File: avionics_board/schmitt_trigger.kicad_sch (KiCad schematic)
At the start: 3 parts, among them U55 74LVC2G07

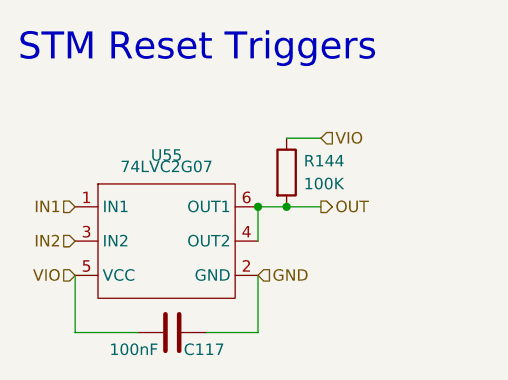
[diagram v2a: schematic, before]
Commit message: cleaning up bom: remove main camera port since it has not pullups and capacitors, correcting some errors in camera switch
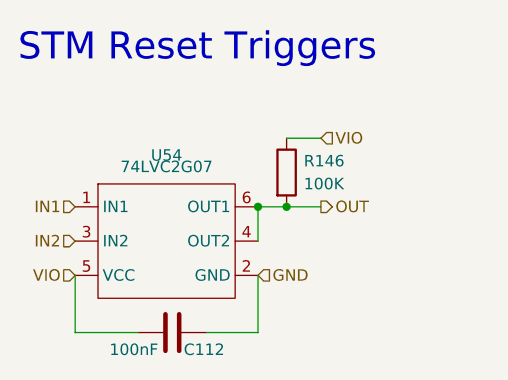
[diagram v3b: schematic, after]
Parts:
- renumbered C117 to C112, R144 to R146, U55 to U54
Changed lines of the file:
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@@
 		(dnp no)
 		(fields_autoplaced yes)
-		(property "Reference" "U55"
+		(property "Reference" "U54"
 			(at 214.63 69.85 0)
 			(effects
@@
 		)
 		(property "Color" ""
+			(at 214.63 79.375 0)
+			(effects
+				(font
+					(size 1.27 1.27)
+				)
+				(hide yes)
+			)
+		)
+		(property "MANUFACTURER" ""
+			(at 214.63 79.375 0)
+			(effects
+				(font
+					(size 1.27 1.27)
+				)
+				(hide yes)
+			)
+		)
+		(property "MAXIMUM_PACKAGE_HEIGHT" ""
+			(at 214.63 79.375 0)
+			(effects
+				(font
+					(size 1.27 1.27)
+				)
+				(hide yes)
+			)
+		)
+		(property "Manufactorer" ""
+			(at 214.63 79.375 0)
+			(effects
+				(font
+					(size 1.27 1.27)
+				)
+				(hide yes)
+			)
+		)
+		(property "PARTREV" ""
+			(at 214.63 79.375 0)
+			(effects
+				(font
+					(size 1.27 1.27)
+				)
+				(hide yes)
+			)
+		)
+		(property "STANDARD" ""
 			(at 214.63 79.375 0)
 			(effects
@@
 			(project "EPS"
 				(path "/05170af6-30ef-4c3a-b972-f098085da1bc/3cb52b52-bdd8-455c-8cb1-f3a303a9432e"
-					(reference "U55")
+					(reference "U54")
 					(unit 1)
 				)
@@
 		(on_board yes)
 		(dnp no)
-		(property "Reference" "C117"
+		(property "Reference" "C112"
 			(at 216.535 91.44 90)
 			(effects
@@
 		)
 		(property "Color" ""
+			(at 215.265 89.535 0)
+			(effects
+				(font
+					(size 1.27 1.27)
+				)
+				(hide yes)
+			)
+		)
+		(property "MANUFACTURER" ""
+			(at 215.265 89.535 0)
+			(effects
+				(font
+					(size 1.27 1.27)
+				)
+				(hide yes)
+			)
+		)
+		(property "MAXIMUM_PACKAGE_HEIGHT" ""
+			(at 215.265 89.535 0)
+			(effects
+				(font
+					(size 1.27 1.27)
+				)
+				(hide yes)
+			)
+		)
+		(property "Manufactorer" ""
+			(at 215.265 89.535 0)
+			(effects
+				(font
+					(size 1.27 1.27)
+				)
+				(hide yes)
+			)
+		)
+		(property "PARTREV" ""
+			(at 215.265 89.535 0)
+			(effects
+				(font
+					(size 1.27 1.27)
+				)
+				(hide yes)
+			)
+		)
+		(property "STANDARD" ""
 			(at 215.265 89.535 0)
 			(effects
@@
 			(project "EPS"
 				(path "/05170af6-30ef-4c3a-b972-f098085da1bc/3cb52b52-bdd8-455c-8cb1-f3a303a9432e"
-					(reference "C117")
+					(reference "C112")
 					(unit 1)
 				)
@@
 		(dnp no)
 		(fields_autoplaced yes)
-		(property "Reference" "R144"
+		(property "Reference" "R146"
 			(at 229.87 70.4849 0)
 			(effects
@@
 		)
 		(property "Color" ""
+			(at 227.965 71.755 0)
+			(effects
+				(font
+					(size 1.27 1.27)
+				)
+				(hide yes)
+			)
+		)
+		(property "MANUFACTURER" ""
+			(at 227.965 71.755 0)
+			(effects
+				(font
+					(size 1.27 1.27)
+				)
+				(hide yes)
+			)
+		)
+		(property "MAXIMUM_PACKAGE_HEIGHT" ""
+			(at 227.965 71.755 0)
+			(effects
+				(font
+					(size 1.27 1.27)
+				)
+				(hide yes)
+			)
+		)
+		(property "Manufactorer" ""
+			(at 227.965 71.755 0)
+			(effects
+				(font
+					(size 1.27 1.27)
+				)
+				(hide yes)
+			)
+		)
+		(property "PARTREV" ""
+			(at 227.965 71.755 0)
+			(effects
+				(font
+					(size 1.27 1.27)
+				)
+				(hide yes)
+			)
+		)
+		(property "STANDARD" ""
 			(at 227.965 71.755 0)
 			(effects
@@
 			(project "EPS"
 				(path "/05170af6-30ef-4c3a-b972-f098085da1bc/3cb52b52-bdd8-455c-8cb1-f3a303a9432e"
-					(reference "R144")
+					(reference "R146")
 					(unit 1)
 				)
@@
 			(project "sci_board"
 				(path "/b4b2c88d-f6cd-4e60-862d-e21f68728580/840799ac-4fe6-4a8e-96a2-299affeec8e4/be725391-4517-4a91-8537-5b0e0ace46a2"
-					(reference "R34")
-					(unit 1)
-				)
+					(reference "R40")
+					(unit 1)
+				)

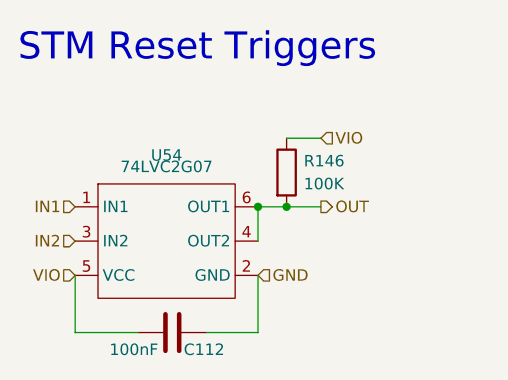
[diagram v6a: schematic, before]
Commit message: local switches and monitors for SCI and RF
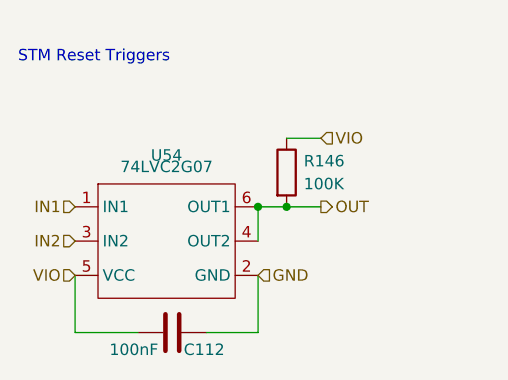
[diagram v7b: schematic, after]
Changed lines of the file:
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@@
 		(effects
 			(font
-				(size 2.9972 2.9972)
+				(size 1.27 1.27)
 			)
 			(justify left bottom)
@@
 			(project "openlst-hw"
 				(path "/a863a5ec-a5d4-4f54-be53-e8c01d5e3ac4/53f12969-e593-459a-9671-cc23a5a9aea0/f4ff56ce-2fa2-4b99-a709-c113709260c1/3711f4d8-fcd4-4aaf-a727-d534b54827fd"
-					(reference "U11")
+					(reference "U18")
 					(unit 1)
 				)
@@
 			(project "sci_board"
 				(path "/b4b2c88d-f6cd-4e60-862d-e21f68728580/840799ac-4fe6-4a8e-96a2-299affeec8e4/be725391-4517-4a91-8537-5b0e0ace46a2"
-					(reference "U24")
+					(reference "U26")
 					(unit 1)
 				)
@@
 			(project "openlst-hw"
 				(path "/a863a5ec-a5d4-4f54-be53-e8c01d5e3ac4/53f12969-e593-459a-9671-cc23a5a9aea0/f4ff56ce-2fa2-4b99-a709-c113709260c1/3711f4d8-fcd4-4aaf-a727-d534b54827fd"
-					(reference "C58")
+					(reference "C68")
 					(unit 1)
 				)
@@
 			(project "sci_board"
 				(path "/b4b2c88d-f6cd-4e60-862d-e21f68728580/840799ac-4fe6-4a8e-96a2-299affeec8e4/be725391-4517-4a91-8537-5b0e0ace46a2"
-					(reference "C57")
+					(reference "C60")
 					(unit 1)
 				)
@@
 			(project "openlst-hw"
 				(path "/a863a5ec-a5d4-4f54-be53-e8c01d5e3ac4/53f12969-e593-459a-9671-cc23a5a9aea0/f4ff56ce-2fa2-4b99-a709-c113709260c1/3711f4d8-fcd4-4aaf-a727-d534b54827fd"
-					(reference "R27")
+					(reference "R41")
 					(unit 1)
 				)
@@
 			(project "sci_board"
 				(path "/b4b2c88d-f6cd-4e60-862d-e21f68728580/840799ac-4fe6-4a8e-96a2-299affeec8e4/be725391-4517-4a91-8537-5b0e0ace46a2"
-					(reference "R40")
-					(unit 1)
-				)
+					(reference "R45")
+					(unit 1)
+				)
